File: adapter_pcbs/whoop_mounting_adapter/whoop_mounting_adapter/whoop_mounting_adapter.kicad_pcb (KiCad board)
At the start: 2 copper layers, 28.8 x 28.9 mm, 16 parts

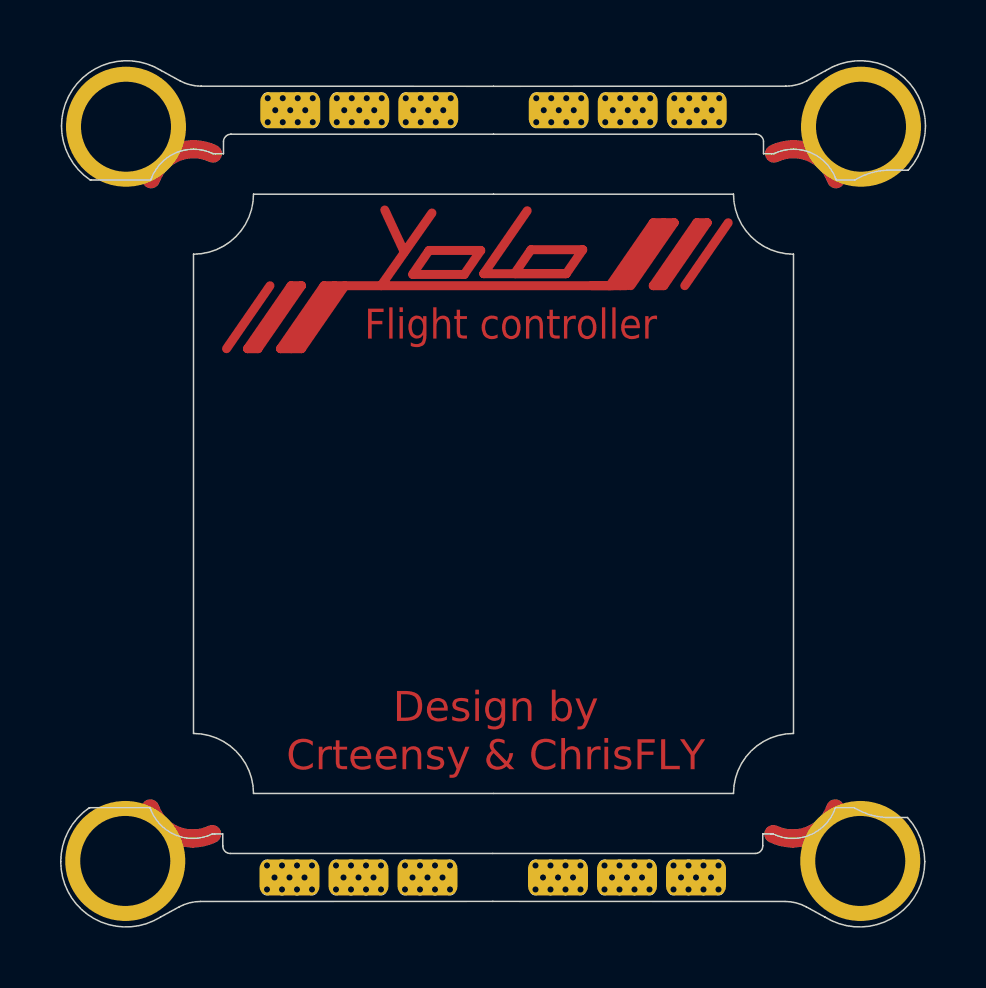
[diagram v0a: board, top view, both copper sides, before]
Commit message: added diode on 5V DCDC input
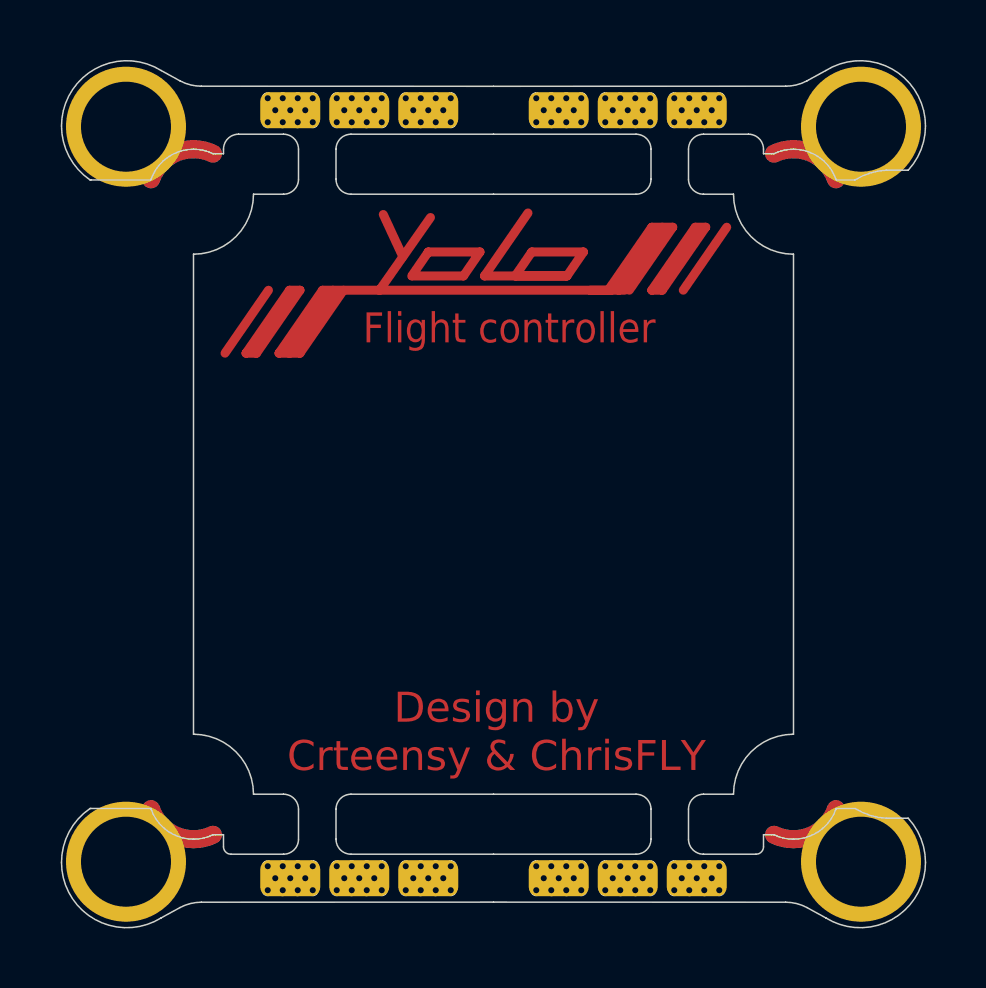
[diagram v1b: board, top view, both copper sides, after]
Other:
- outline, holes or cut-outs redrawn
